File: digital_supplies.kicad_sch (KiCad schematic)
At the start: 58 parts, among them Q1 PMOS, Q2 2PNP, Q4 2NPN, Q8 PMOS, U19 74LVC1G06, U4 3V3REG, U5 LDO-ADJ, U6 LDO-ADJ, U7 LDO-ADJ

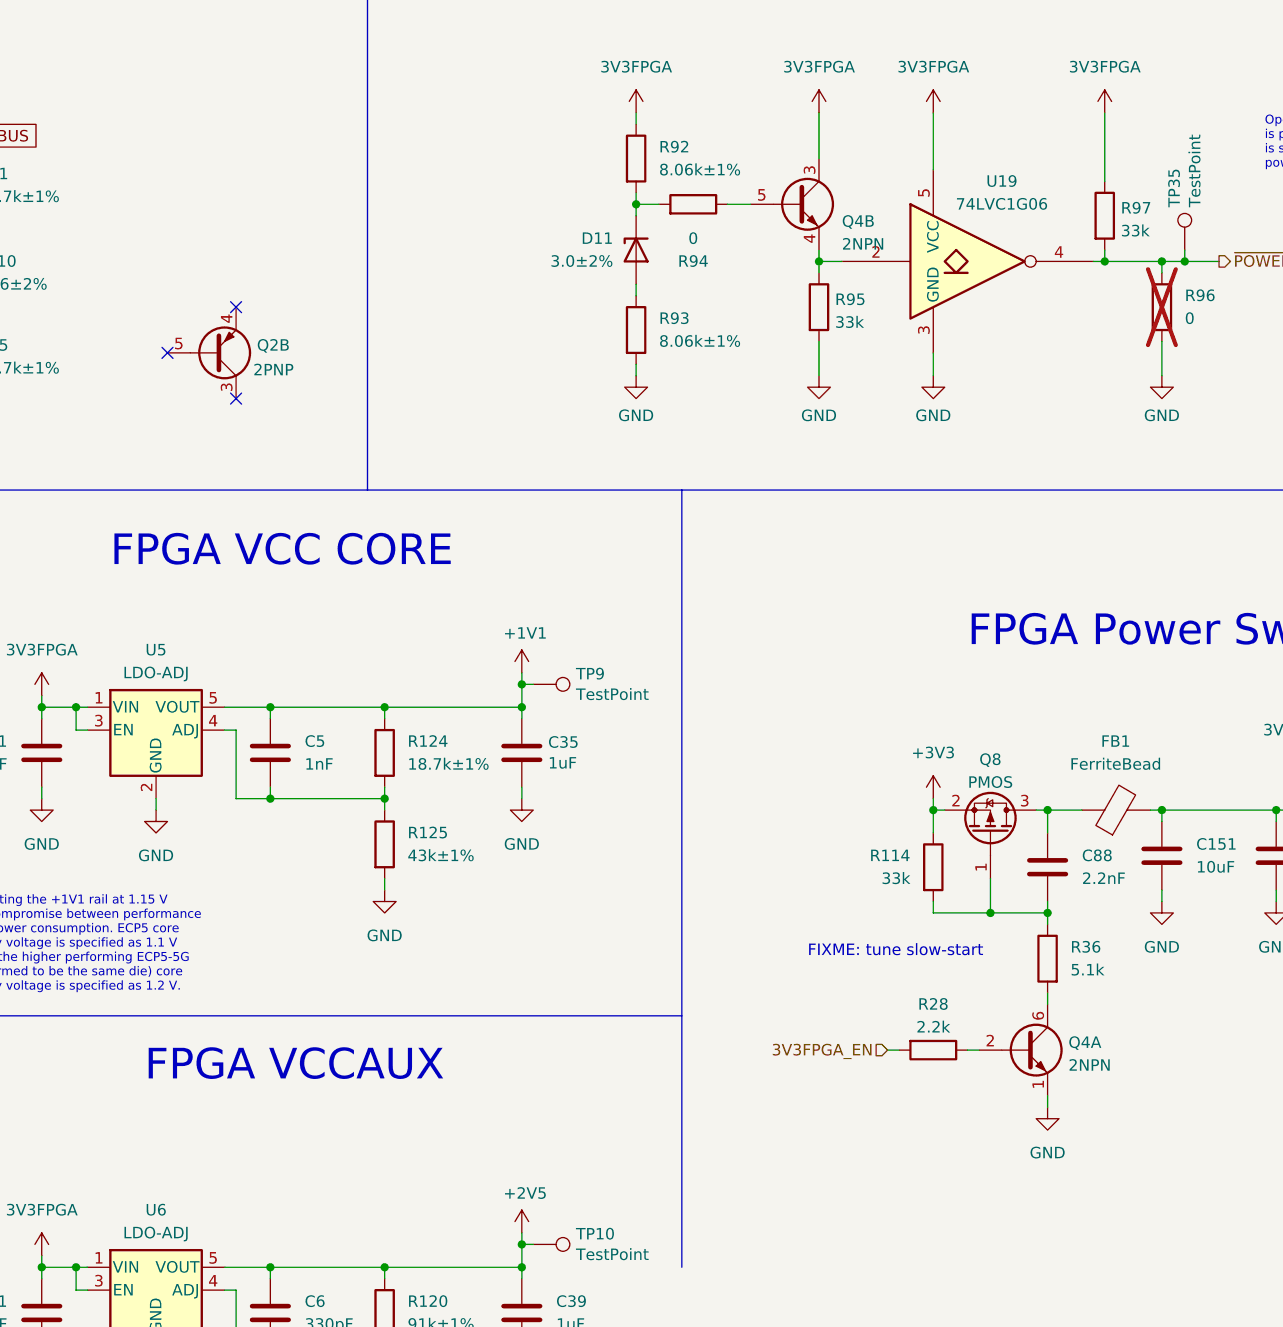
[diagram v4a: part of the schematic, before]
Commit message: invert 3V3FPGA_EN
The mcu has default pull-up, not pull-down.
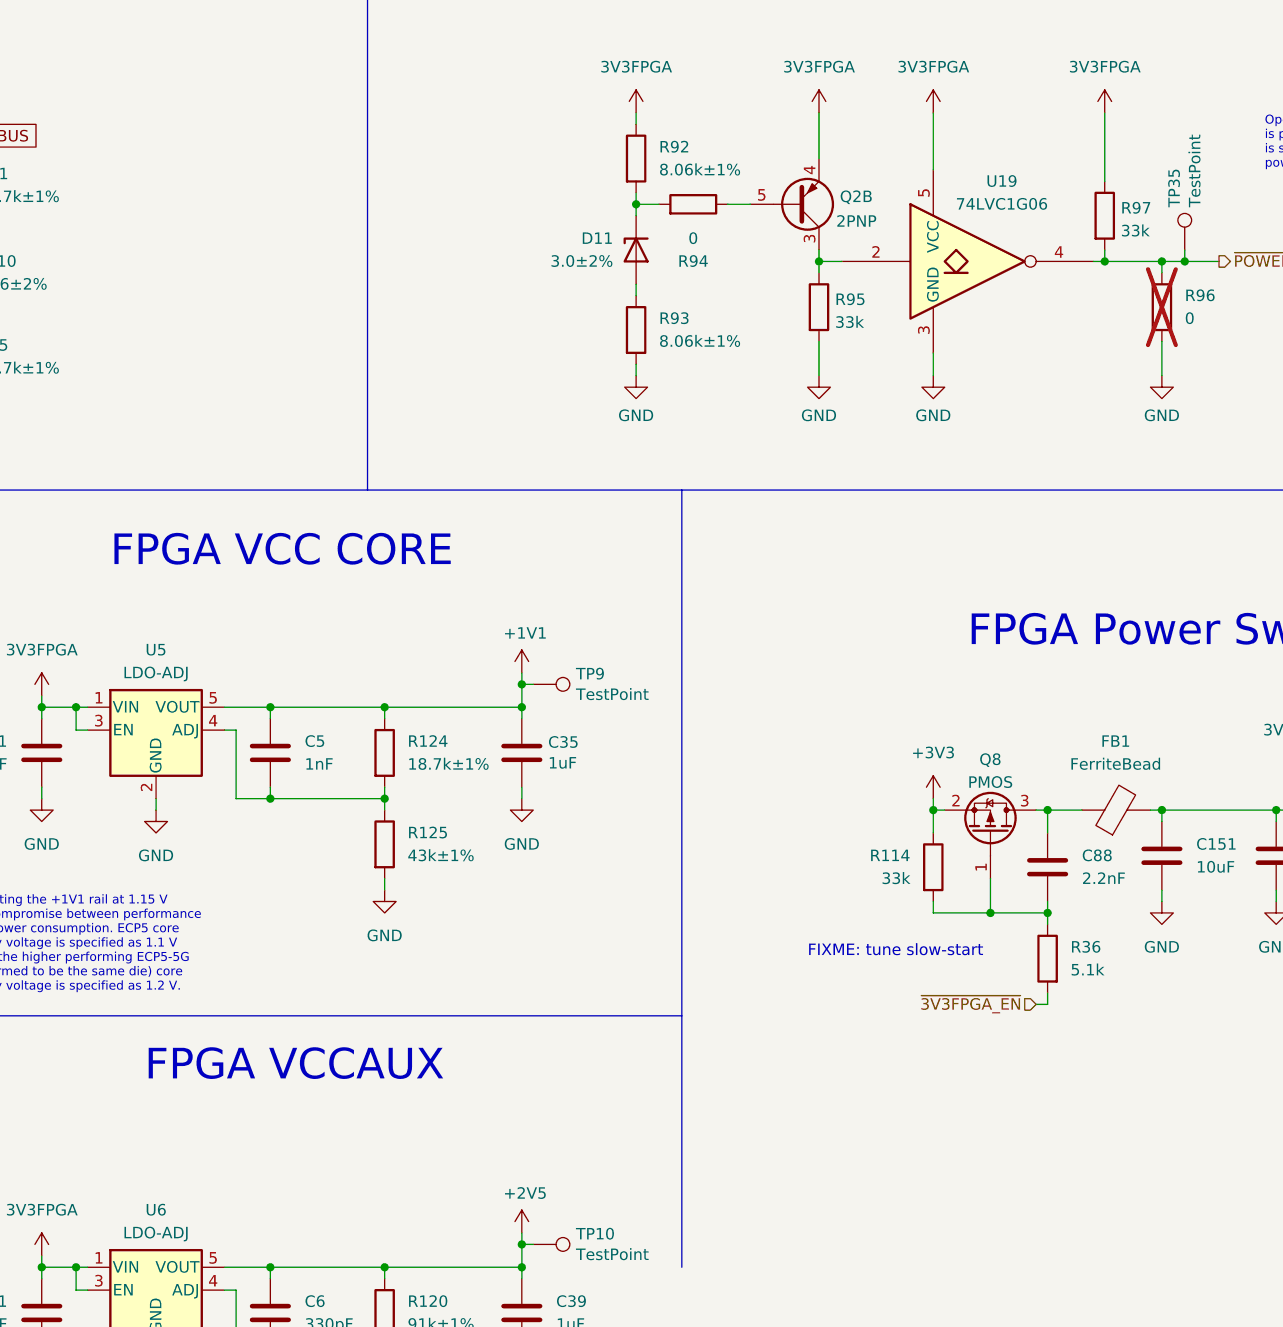
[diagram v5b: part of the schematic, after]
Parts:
- removed Q4: 2NPN, Package_TO_SOT_SMD:SOT-363_SC-70-6, symbol Transistor_BJT:BC847BS
- removed R28: 2.2k, Resistor_SMD:R_0402_1005Metric, symbol Device:R
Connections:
- net 3V3FPGA: now also Q2.4 (E2)
- net at Q2.3 (C2): now also R95.1, U19.2
- net at Q2.5 (B2): now also R94.1
- net ~{3V3FPGA_EN}: now reaches R36.2
- no-connect marks 3 -> 0
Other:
- moved on the sheet: Q2B

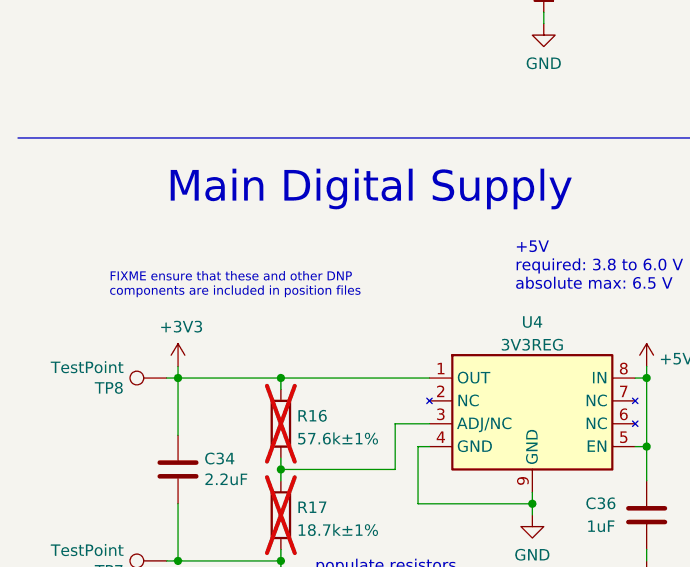
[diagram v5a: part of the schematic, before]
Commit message: include all components in position file
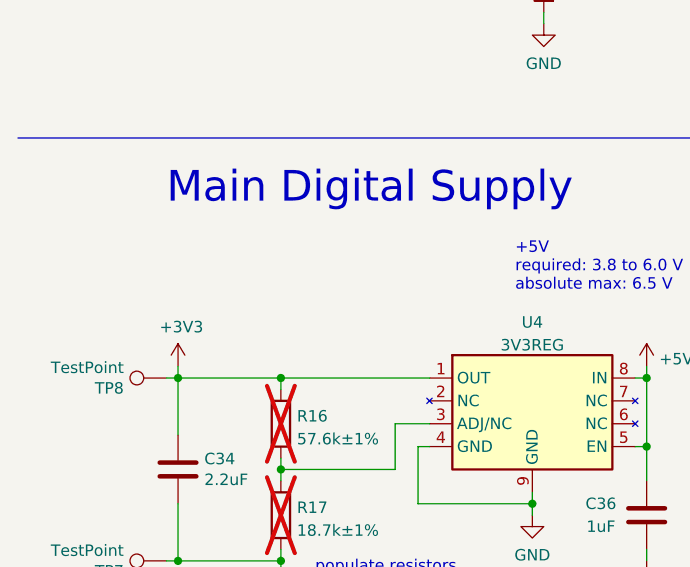
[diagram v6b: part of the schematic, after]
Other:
- note removed: "FIXME ensure that these and other DNP components are included in position files"
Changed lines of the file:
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@@
     (effects (font (size 1.27 1.27)) (justify left bottom))
-  )
-  (text "FIXME ensure that these and other DNP\ncomponents are included in position files"
-    (at 22.86 96.52 0)
-    (effects (font (size 0.9906 0.9906)) (justify left bottom))
   )
   (text "FPGA Power Switch" (at 209.55 96.52 0)
